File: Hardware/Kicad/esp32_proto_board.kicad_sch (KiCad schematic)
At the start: 12 parts, among them J13 Edge_Pads_Right_Top, J15 Edge_Pads_Right_Bottom, J23 Edge_Pads_Left_Top, J24 Edge_Pads_Left_Bottom

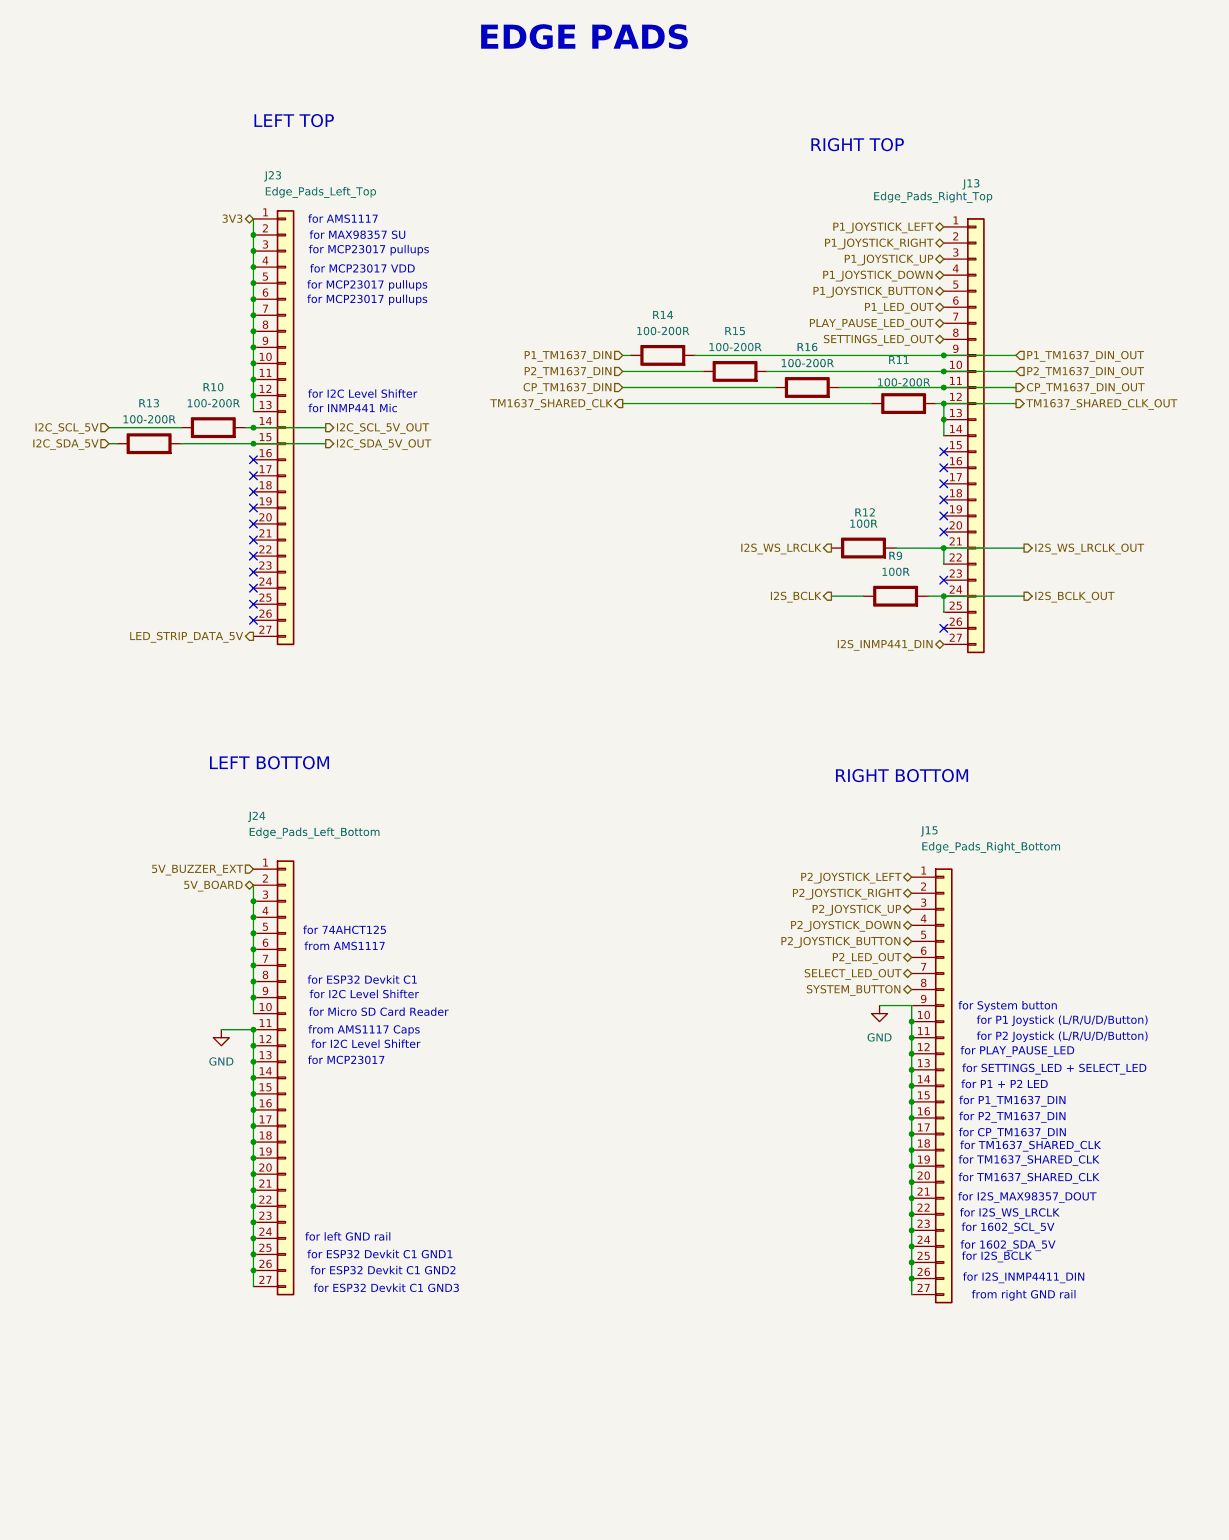
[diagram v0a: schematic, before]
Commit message: Replaced 1602 to 2004 in Kicad and Tinkercad
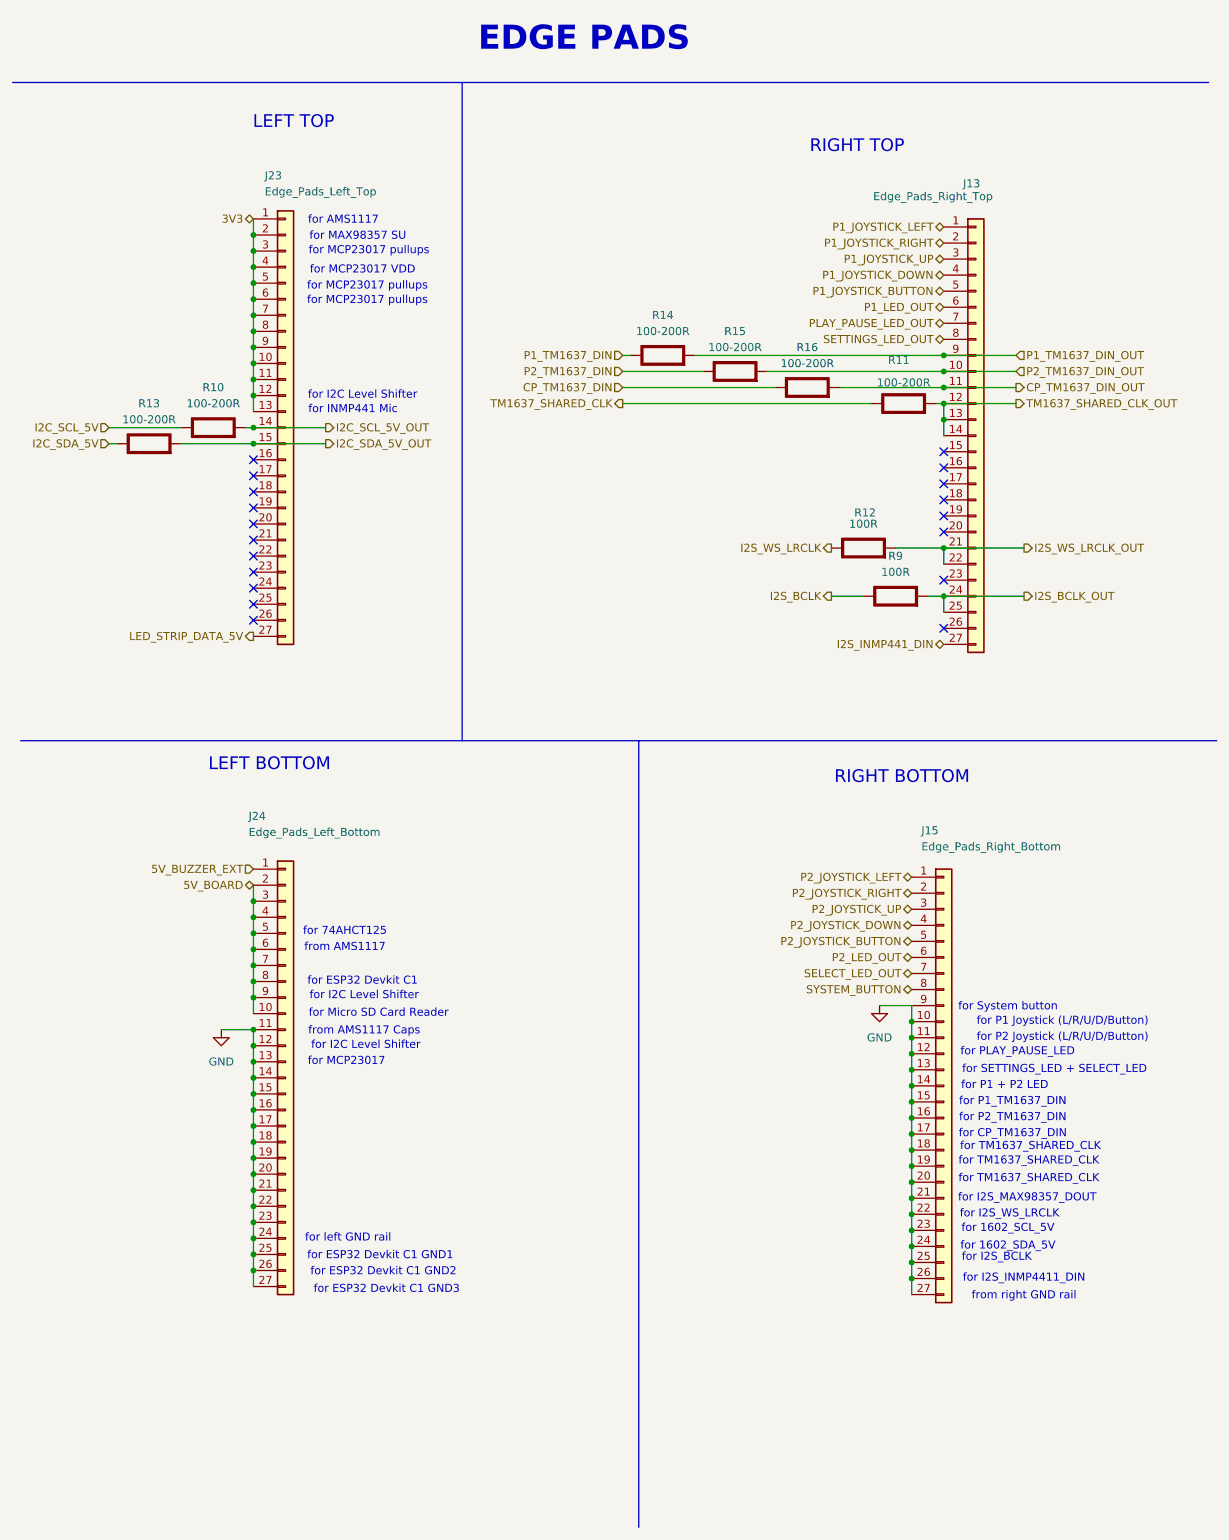
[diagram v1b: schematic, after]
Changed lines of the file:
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@@
+		)
+	)
+	(polyline
+		(pts
+			(xy 10.16 25.4) (xy 199.39 25.4)
+		)
+		(stroke
+			(width 0)
+			(type default)
 		)
 	)
@@
 		)
 	)
+	(polyline
+		(pts
+			(xy 109.22 254) (xy 109.22 129.54)
+		)
+		(stroke
+			(width 0)
+			(type default)
+		)
+	)
 	(wire
 		(pts
@@
 		)
 	)
+	(polyline
+		(pts
+			(xy 11.43 129.54) (xy 200.66 129.54)
+		)
+		(stroke
+			(width 0)
+			(type default)
+		)
+	)
 	(wire
 		(pts
@@
 		)
 		(stroke
+			(width 0)
+			(type default)
+		)
+	)
+	(polyline
+		(pts
+			(xy 81.28 129.54) (xy 81.28 25.4)
+		)
+		(stroke

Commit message: Broken code, halfway joystick gdi
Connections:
- net HC_SR04_ECHO_1: now reaches J23.16 (Pin_16)
- net HC_SR04_TRIG_1: now reaches J23.17 (Pin_17)
- net HC_SR04_ECHO_2: now reaches J23.18 (Pin_18)
- net HC_SR04_TRIG_2: now reaches J23.19 (Pin_19)
- net HC_SR04_ECHO_3: now reaches J23.20 (Pin_20)
- net HC_SR04_TRIG_3: now reaches J23.21 (Pin_21)
- net HC_SR04_ECHO_4: now reaches J23.22 (Pin_22)
- net HC_SR04_TRIG_4: now reaches J23.23 (Pin_23)
- no-connect marks 19 -> 11
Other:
- note added: "for HC-SR04 Level Shifter"
- note added: "for HC-SR05 1"
- note added: "for HC-SR05 2"
- note added: "for HC-SR05 3"
- note added: "for HC-SR05 4"
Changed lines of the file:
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@@
+		)
+	)
+	(text "for HC-SR05 1"
+		(exclude_from_sim no)
+		(at 62.992 182.88 0)
+		(effects
+			(font
+				(size 1.27 1.27)
+			)
 		)
 	)
@@
 		)
 	)
+	(text "for HC-SR05 2"
+		(exclude_from_sim no)
+		(at 63.246 185.42 0)
+		(effects
+			(font
+				(size 1.27 1.27)
+			)
+		)
+	)
 	(text "for P1 + P2 LED"
 		(exclude_from_sim no)
@@
 		)
 	)
+	(text "for HC-SR04 Level Shifter"
+		(exclude_from_sim no)
+		(at 69.342 164.846 0)
+		(effects
+			(font
+				(size 1.27 1.27)
+			)
+		)
+	)
 	(text "RIGHT TOP"
 		(exclude_from_sim no)
@@
 		(exclude_from_sim no)
 		(at 66.294 59.944 0)
+		(effects
+			(font
+				(size 1.27 1.27)
+			)
+		)
+	)
+	(text "for HC-SR05 4"
+		(exclude_from_sim no)
+		(at 63.246 190.754 0)
+		(effects
+			(font
+				(size 1.27 1.27)
+			)
+		)
+	)
+	(text "for HC-SR05 3"
+		(exclude_from_sim no)
+		(at 62.992 188.214 0)
 		(effects
 			(font
@@
 	)
 	(no_connect
-		(at 48.26 90.17)
-	)
-	(no_connect
-		(at 48.26 102.87)
-	)
-	(no_connect
 		(at 157.48 91.44)
 	)
@@
 	)
 	(no_connect
-		(at 48.26 85.09)
-	)
-	(no_connect
 		(at 157.48 111.76)
-	)
-	(no_connect
-		(at 48.26 100.33)
 	)
 	(no_connect
@@
 	)
 	(no_connect
-		(at 48.26 92.71)
-	)
-	(no_connect
 		(at 157.48 88.9)
-	)
-	(no_connect
-		(at 48.26 95.25)
-	)
-	(no_connect
-		(at 48.26 97.79)
 	)
 	(no_connect
 		(at 48.26 107.95)
-	)
-	(no_connect
-		(at 48.26 87.63)
 	)
 	(wire
@@
 		)
 	)
+	(hierarchical_label "HC_SR04_ECHO_2"
+		(shape output)
+		(at 48.26 90.17 180)
+		(effects
+			(font
+				(size 1.27 1.27)
+			)
+			(justify right)
+		)
+	)
 	(hierarchical_label "5V_BUZZER_EXT"
 		(shape input)
@@
 		)
 	)
+	(hierarchical_label "HC_SR04_TRIG_2"
+		(shape input)
+		(at 48.26 92.71 180)
+		(effects
+			(font
+				(size 1.27 1.27)
+			)
+			(justify right)
+		)
+	)
+	(hierarchical_label "HC_SR04_ECHO_4"
+		(shape output)
+		(at 48.26 100.33 180)
+		(effects
+			(font
+				(size 1.27 1.27)
+			)
+			(justify right)
+		)
+	)
 	(hierarchical_label "I2S_BCLK"
 		(shape output)
@@
 		)
 	)
+	(hierarchical_label "HC_SR04_TRIG_3"
+		(shape input)
+		(at 48.26 97.79 180)
+		(effects
+			(font
+				(size 1.27 1.27)
+			)
+			(justify right)
+		)
+	)
+	(hierarchical_label "HC_SR04_ECHO_1"
+		(shape output)
+		(at 48.26 85.09 180)
+		(effects
+			(font
+				(size 1.27 1.27)
+			)
+			(justify right)
+		)
+	)
 	(hierarchical_label "P2_JOYSTICK_UP"
 		(shape bidirectional)
@@
 		)
 	)
+	(hierarchical_label "HC_SR04_ECHO_3"
+		(shape output)
+		(at 48.26 95.25 180)
+		(effects
+			(font
+				(size 1.27 1.27)
+			)
+			(justify right)
+		)
+	)
+	(hierarchical_label "HC_SR04_TRIG_4"
+		(shape input)
+		(at 48.26 102.87 180)
+		(effects
+			(font
+				(size 1.27 1.27)
+			)
+			(justify right)
+		)
+	)
 	(hierarchical_label "P1_TM1637_DIN_OUT"
 		(shape input)
@@
 		(effects
 			(font
+				(size 1.27 1.27)
+			)
+			(justify right)
+		)
+	)
+	(hierarchical_label "HC_SR04_TRIG_1"
+		(shape input)
+		(at 48.26 87.63 180)
+		(effects
+			(font
